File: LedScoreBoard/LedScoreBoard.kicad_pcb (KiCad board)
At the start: 2 copper layers, 145 x 95 mm, 106 parts, among them J1 Conn_01x02_Male, J2 Conn_01x06_Male, J3 Conn_01x02_Male, J4 Conn_01x08_Male, J5 Conn_01x08_Male, J6 Conn_01x08_Male, Q1 BSS84, Q10 BSS84, Q11 BSS138, Q12 BSS84, Q13 BSS138, Q14 2SJ349, Q15 2SJ349, Q16 2SJ349, Q17 TK40E06N1, Q18 TK40E06N1, Q19 TK40E06N1, Q2 BSS84, Q20 TK40E06N1, Q21 BSS138, Q22 BSS138, Q23 BSS138, Q24 BSS138, Q25 TK40E06N1, Q26 TK40E06N1, Q27 TK40E06N1, Q28 BSS138, Q29 BSS138, Q3 BSS84, Q30 BSS138, Q31 BSS138, Q32 BSS138, Q33 BSS138, Q34 BSS138, Q35 BSS138, Q36 BSS138, Q37 BSS138, Q4 BSS138, Q5 BSS138, Q6 BSS138, Q7 BSS138, Q8 BSS84, Q9 BSS138, SW1 SW_Push, SW2 SW_Push, SW3 SW_Push, SW4 SW_Push, SW5 SW_Push, SW6 SW_Push, U1 PIC16F1516-ISP, U2 LM2931-3.3_TO220, U3 LM358, U4 LM358, U5 LM358, U6 LM358

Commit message: SerialTerminal
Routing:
- removed copper zone on F.Cu, net VDD
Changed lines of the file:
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@@
   (segment locked (start 168.91 82.55) (end 163.83 82.55) (width 2) (layer "F.Cu") (net 95))
   (segment locked (start 163.83 66.04) (end 168.91 66.04) (width 2) (layer "F.Cu") (net 96))
-  (zone locked (net 24) (net_name "VDD") (layer "F.Cu") (hatch edge 0.508)
-    (connect_pads (clearance 0.254))
-    (min_thickness 0.254) (filled_areas_thickness no)
-    (fill yes (thermal_gap 0.508) (thermal_bridge_width 0.508))
-    (polygon
-      (pts
-        (xy 161.29 97.79)
-        (xy 156.21 97.79)
-        (xy 156.21 49.53)
-        (xy 161.29 49.53)
-      )
-    )
-  )
   (group "" (id 08d3dc0f-4c91-49b0-ac90-7a56e69acdb1)
     (members

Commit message: 配置ブロック決定
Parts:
- removed C1, C5, C6, C7, C8: 0.1u, Capacitor_SMD:C_0603_1608Metric
- removed C2: 1u, Capacitor_SMD:C_0603_1608Metric
- removed C3, C4: 10u, Capacitor_SMD:C_0603_1608Metric
- removed D1: GDZJ112C, Diode_SMD:D_TUMD2
- removed D2, D3, D4: ER504, Diode_THT:D_DO-27_P5.08mm_Vertical_AnodeUp
- removed DS1: 2831BS-RIGHT-ANGLE, 2831BS-RIGHT-ANGLE:DIPS762W45P254L2253H610Q12N
- removed J1, J3: Conn_01x02_Male, TerminalBlock:TerminalBlock_bornier-2_P5.08mm
- removed J2: Conn_01x06_Male, Connector_PinHeader_2.54mm:PinHeader_1x06_P2.54mm_Vertical
- removed J4, J5, J6: Conn_01x08_Male, Connector_JST:JST_VH_B8P-VH_1x08_P3.96mm_Vertical
- removed Q1, Q10, Q12, Q2, Q3, Q8: BSS84, Package_TO_SOT_SMD:SOT-23_Handsoldering
- removed Q11, Q13, Q21, Q22, Q23, Q24, Q28, Q29, Q30, Q31, Q32, Q33, Q34, Q35, Q36, Q37, Q4, Q5, Q6, Q7, Q9: BSS138, Package_TO_SOT_SMD:SOT-23_Handsoldering
- removed Q14, Q15, Q16: 2SJ349, Package_TO_SOT_THT:TO-220-3_Vertical
- removed Q17, Q18, Q19, Q20, Q25, Q26, Q27: TK40E06N1, Package_TO_SOT_THT:TO-220-3_Vertical
- removed R1, R19, R2, R20, R21, R22, R3, R30, R31, R32, R4, R5, R6, R7: 1k, Resistor_SMD:R_0603_1608Metric
- removed R10, R12, R8: 3.3k, Resistor_SMD:R_0603_1608Metric
- removed R11, R13, R14, R9: 10k, Resistor_SMD:R_0603_1608Metric
- removed R15, R16, R17, R18, R27, R28, R29, R36, R37, R38: 20, Resistor_SMD:R_0603_1608Metric
- removed R23, R24, R25, R26, R33, R34, R35: 1.0, Resistor_SMD:R_2512_6332Metric_Pad1.40x3.35mm_HandSolder
- removed SW1, SW2, SW3, SW4, SW5, SW6: SW_Push, Button_Switch_THT:SW_PUSH_6mm
- removed U1: PIC16F1516-ISP, Package_DIP:DIP-28_W7.62mm_Socket_LongPads
- removed U2: LM2931-3.3_TO220, Package_TO_SOT_THT:TO-220-3_Vertical
- removed U3, U4, U5, U6: LM358, Package_SO:TSSOP-8_3x3mm_P0.65mm
- added C101: 0.1u, Capacitor_SMD:C_0603_1608Metric, F.Cu at (-23.6, 277.4)
- added C102: 0.1u, Capacitor_SMD:C_0603_1608Metric, F.Cu at (24.8, 60.3)
- added C103: 10u, Capacitor_SMD:C_0603_1608Metric, F.Cu at (1.06, 257.0)
- added C104: 10u, Capacitor_SMD:C_0603_1608Metric, F.Cu at (-62.3, 293.9)
- added C201: 1u, Capacitor_SMD:C_0603_1608Metric, B.Cu at (110.2, 30.5)
- added C301: 1u, Capacitor_SMD:C_0603_1608Metric, B.Cu at (35.6, 144.8)
- added C302: 1u, Capacitor_SMD:C_0603_1608Metric, B.Cu at (63.5, 144.8)
- added C303: 1u, Capacitor_SMD:C_0603_1608Metric, B.Cu at (76.2, 144.8)
- added C304: 1u, Capacitor_SMD:C_0603_1608Metric, B.Cu at (104.1, 144.8)
- added C305: 1u, Capacitor_SMD:C_0603_1608Metric, B.Cu at (116.8, 144.8)
- added C306: 1u, Capacitor_SMD:C_0603_1608Metric, B.Cu at (144.8, 144.8)
- added C307: 1u, Capacitor_SMD:C_0603_1608Metric, B.Cu at (157.5, 144.8)
- added C308: 0.1u, Capacitor_SMD:C_0603_1608Metric, B.Cu at (29.2, 152.4)
- added C309: 0.1u, Capacitor_SMD:C_0603_1608Metric, B.Cu at (69.8, 152.4)
- added C310: 0.1u, Capacitor_SMD:C_0603_1608Metric, B.Cu at (110.5, 152.4)
- added C311: 0.1u, Capacitor_SMD:C_0603_1608Metric, B.Cu at (151.1, 152.4)
- added D201: UDZV12B, Diode_SMD:D_TUMD2, B.Cu at (106.3, 30.5)
- added D202: ER504, Diode_THT:D_DO-27_P5.08mm_Vertical_AnodeUp, F.Cu at (125.4, 50.8)
- added D203: ER504, Diode_THT:D_DO-27_P5.08mm_Vertical_AnodeUp, F.Cu at (125.4, 76.2)
- added D204: ER504, Diode_THT:D_DO-27_P5.08mm_Vertical_AnodeUp, F.Cu at (125.4, 101.6)
- added I2C101: Conn_01x04_Male, Connector_PinHeader_2.54mm:PinHeader_1x04_P2.54mm_Vertical, F.Cu at (-23.3, 286.3)
- added J101: LCD, Connector_PinSocket_2.54mm:PinSocket_1x07_P2.54mm_Vertical, F.Cu at (-27.9, 278.5)
- added J102: 1, Connector_JST:JST_VH_B8P-VH_1x08_P3.96mm_Vertical, F.Cu at (137.2, 50.8)
- added J103: 10, Connector_JST:JST_VH_B8P-VH_1x08_P3.96mm_Vertical, F.Cu at (137.2, 76.2)
- added J104: 100, Connector_JST:JST_VH_B8P-VH_1x08_P3.96mm_Vertical, F.Cu at (137.2, 101.6)
- added J105: DC12_IN, TerminalBlock:TerminalBlock_bornier-2_P5.08mm, F.Cu at (-49.5, 291.2)
- added J106: VDD_IN, TerminalBlock:TerminalBlock_bornier-2_P5.08mm, F.Cu at (2.29, 251.2)
- added J107: PICkit, Connector_PinHeader_2.54mm:PinHeader_1x06_P2.54mm_Vertical, F.Cu at (-94.0, 316.2)
- added Q201: BSS138, Package_TO_SOT_SMD:SOT-23_Handsoldering, B.Cu at (86.0, 54.6)
- added Q202: BSS84, Package_TO_SOT_SMD:SOT-23_Handsoldering, B.Cu at (96.2, 47.0)
- added Q203: BSS138, Package_TO_SOT_SMD:SOT-23_Handsoldering, B.Cu at (96.2, 54.6)
- added Q204: 2SJ349, Package_TO_SOT_THT:TO-220-3_Vertical, F.Cu at (108.9, 50.8)
- added Q205: BSS138, Package_TO_SOT_SMD:SOT-23_Handsoldering, B.Cu at (86.0, 80.0)
- added Q206: BSS84, Package_TO_SOT_SMD:SOT-23_Handsoldering, B.Cu at (96.2, 72.4)
- added Q207: BSS138, Package_TO_SOT_SMD:SOT-23_Handsoldering, B.Cu at (96.2, 80.0)
- added Q208: 2SJ349, Package_TO_SOT_THT:TO-220-3_Vertical, F.Cu at (108.9, 76.2)
- added Q209: BSS138, Package_TO_SOT_SMD:SOT-23_Handsoldering, B.Cu at (86.0, 105.4)
- added Q210: BSS84, Package_TO_SOT_SMD:SOT-23_Handsoldering, B.Cu at (96.2, 97.8)
- added Q211: BSS138, Package_TO_SOT_SMD:SOT-23_Handsoldering, B.Cu at (96.2, 105.4)
- added Q212: 2SJ349, Package_TO_SOT_THT:TO-220-3_Vertical, F.Cu at (108.9, 101.6)
- added Q301: BSS138, Package_TO_SOT_SMD:SOT-23_Handsoldering, B.Cu at (35.6, 138.4)
- added Q302: TK40E06N1, Package_TO_SOT_THT:TO-220-3_Vertical, F.Cu at (41.9, 160.0)
- added Q303: BSS138, Package_TO_SOT_SMD:SOT-23_Handsoldering, B.Cu at (63.5, 138.4)
- added Q304: TK40E06N1, Package_TO_SOT_THT:TO-220-3_Vertical, F.Cu at (62.2, 160.0)
- added Q305: BSS138, Package_TO_SOT_SMD:SOT-23_Handsoldering, B.Cu at (76.2, 138.4)
- added Q306: TK40E06N1, Package_TO_SOT_THT:TO-220-3_Vertical, F.Cu at (82.5, 160.0)
- added Q307: BSS138, Package_TO_SOT_SMD:SOT-23_Handsoldering, B.Cu at (104.1, 138.4)
- added Q308: TK40E06N1, Package_TO_SOT_THT:TO-220-3_Vertical, F.Cu at (102.9, 160.0)
- added Q309: BSS138, Package_TO_SOT_SMD:SOT-23_Handsoldering, B.Cu at (116.8, 138.4)
- added Q310: TK40E06N1, Package_TO_SOT_THT:TO-220-3_Vertical, F.Cu at (143.5, 160.0)
- added Q311: BSS138, Package_TO_SOT_SMD:SOT-23_Handsoldering, B.Cu at (144.8, 138.4)
- added Q312: TK40E06N1, Package_TO_SOT_THT:TO-220-3_Vertical, F.Cu at (123.2, 160.0)
- added Q313: BSS138, Package_TO_SOT_SMD:SOT-23_Handsoldering, B.Cu at (157.5, 138.4)
- added Q314: TK40E06N1, Package_TO_SOT_THT:TO-220-3_Vertical, F.Cu at (163.8, 160.0)
- added R201: 3.3k, Resistor_SMD:R_0603_1608Metric, B.Cu at (91.1, 47.0)
- added R202: 10k, Resistor_SMD:R_0603_1608Metric, B.Cu at (91.1, 54.6)
- added R203: 10k, Resistor_SMD:R_0603_1608Metric, B.Cu at (112.7, 30.5)
- added R204: 20, Resistor_SMD:R_0603_1608Metric, B.Cu at (102.5, 50.8)
- added R205: 3.3k, Resistor_SMD:R_0603_1608Metric, B.Cu at (91.1, 72.4)
- added R206: 10k, Resistor_SMD:R_0603_1608Metric, B.Cu at (91.1, 80.0)
- added R207: 20, Resistor_SMD:R_0603_1608Metric, B.Cu at (102.5, 76.2)
- added R208: 3.3k, Resistor_SMD:R_0603_1608Metric, B.Cu at (91.1, 97.8)
- added R209: 10k, Resistor_SMD:R_0603_1608Metric, B.Cu at (91.1, 105.4)
- added R210: 20, Resistor_SMD:R_0603_1608Metric, B.Cu at (102.5, 101.6)
- added R301: 20, Resistor_SMD:R_0603_1608Metric, B.Cu at (35.6, 149.9)
- added R302: 1k, Resistor_SMD:R_0603_1608Metric, B.Cu at (35.6, 147.3)
- added R303: 1.0, Resistor_SMD:R_2512_6332Metric_Pad1.40x3.35mm_HandSolder, B.Cu at (29.2, 160.0)
- added R304: 20, Resistor_SMD:R_0603_1608Metric, B.Cu at (63.5, 149.9)
- added R305: 1k, Resistor_SMD:R_0603_1608Metric, B.Cu at (63.5, 147.3)
- added R306: 1.0, Resistor_SMD:R_2512_6332Metric_Pad1.40x3.35mm_HandSolder, B.Cu at (49.5, 160.0)
- added R307: 20, Resistor_SMD:R_0603_1608Metric, B.Cu at (76.2, 149.9)
- added R308: 1k, Resistor_SMD:R_0603_1608Metric, B.Cu at (76.2, 147.3)
- added R309: 1.0, Resistor_SMD:R_2512_6332Metric_Pad1.40x3.35mm_HandSolder, B.Cu at (69.8, 160.0)
- added R310: 20, Resistor_SMD:R_0603_1608Metric, B.Cu at (104.1, 149.9)
- added R311: 1k, Resistor_SMD:R_0603_1608Metric, B.Cu at (104.1, 147.3)
- added R312: 1.0, Resistor_SMD:R_2512_6332Metric_Pad1.40x3.35mm_HandSolder, B.Cu at (90.2, 160.0)
- added R313: 20, Resistor_SMD:R_0603_1608Metric, B.Cu at (116.8, 149.9)
- added R314: 1k, Resistor_SMD:R_0603_1608Metric, B.Cu at (116.8, 147.3)
- added R315: 1.0, Resistor_SMD:R_2512_6332Metric_Pad1.40x3.35mm_HandSolder, B.Cu at (110.5, 160.0)
- added R316: 20, Resistor_SMD:R_0603_1608Metric, B.Cu at (144.8, 149.9)
- added R317: 1k, Resistor_SMD:R_0603_1608Metric, B.Cu at (144.8, 147.3)
- added R318: 1.0, Resistor_SMD:R_2512_6332Metric_Pad1.40x3.35mm_HandSolder, B.Cu at (130.8, 160.0)
- added R319: 20, Resistor_SMD:R_0603_1608Metric, B.Cu at (157.5, 149.9)
- added R320: 1k, Resistor_SMD:R_0603_1608Metric, B.Cu at (157.5, 147.3)
- added R321: 1.0, Resistor_SMD:R_2512_6332Metric_Pad1.40x3.35mm_HandSolder, B.Cu at (151.1, 160.0)
- added SW101: SW_Push, Button_Switch_THT:SW_PUSH_6mm, F.Cu at (12.6, 248.7)
- added SW102: PlusHun, Button_Switch_THT:SW_PUSH_6mm, F.Cu at (50.8, 91.4)
- added SW103: MinusHun, Button_Switch_THT:SW_PUSH_6mm, F.Cu at (50.8, 101.6)
- added SW104: PlusTen, Button_Switch_THT:SW_PUSH_6mm, F.Cu at (62.2, 91.4)
- added SW105: MinusTen, Button_Switch_THT:SW_PUSH_6mm, F.Cu at (62.2, 101.6)
- added SW106: PlusOne, Button_Switch_THT:SW_PUSH_6mm, F.Cu at (73.7, 91.4)
- added SW107: MinusOne, Button_Switch_THT:SW_PUSH_6mm, F.Cu at (73.7, 101.6)
- added U101: PIC16F1516-ISP, Package_DIP:DIP-28_W7.62mm_Socket_LongPads, F.Cu at (33.0, 121.9)
- added U102: MW-R-WX, MonoWireless:MonoWireless_TWELITE-SMD_SMA-Connector, F.Cu at (38.1, 99.1)
- added U103: LM2931-3.3_TO220, Package_TO_SOT_THT:TO-220-3_Vertical, F.Cu at (-61.1, 290.6)
- added U301: LM358, Package_SO:TSSOP-8_3x3mm_P0.65mm, B.Cu at (29.2, 148.6)
- added U302: LM358, Package_SO:TSSOP-8_3x3mm_P0.65mm, B.Cu at (69.8, 148.6)
- added U303: LM358, Package_SO:TSSOP-8_3x3mm_P0.65mm, B.Cu at (110.5, 148.6)
- added U304: LM358, Package_SO:TSSOP-8_3x3mm_P0.65mm, B.Cu at (151.1, 148.6)
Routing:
- net VDD: track 10.2 -> 0.00 mm
- net /anodeTen: track 8.89 -> 0.00 mm
- net /anodeHun: track 8.89 -> 0.00 mm
- net /anodeOne: track 8.44 -> 0.00 mm
- net Net-(D2-Pad2): track 5.53 -> 0.00 mm
- net Net-(D4-Pad2): track 5.08 -> 0.00 mm
- net Net-(D3-Pad2): track 5.08 -> 0.00 mm
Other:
- board size 145 x 95 mm -> 149.9 x 149.9 mm

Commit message: パターン完成
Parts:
- added J108: TweLite-R, Connector_PinHeader_2.54mm:PinHeader_1x06_P2.54mm_Vertical, F.Cu at (27.9, 78.7)
- added REF01: MountingHole_3.2mm_M3, MountingHole:MountingHole_3.2mm_M3, F.Cu at (25.4, 30.5)
- added REF02: MountingHole_3.2mm_M3, MountingHole:MountingHole_3.2mm_M3, F.Cu at (165.1, 30.5)
- added REF03: MountingHole_3.2mm_M3, MountingHole:MountingHole_3.2mm_M3, F.Cu at (25.4, 170.2)
- added REF04: MountingHole_3.2mm_M3, MountingHole:MountingHole_3.2mm_M3, F.Cu at (165.1, 170.2)
- added REF05: MountingHole_6.4mm_M6, MountingHole:MountingHole_6.4mm_M6, F.Cu at (43.2, 38.1)
- C101, C102, C103, C104: moved to B.Cu
- D202, D203, D204: footprint Diode_THT:D_DO-27_P5.08mm_Vertical_AnodeUp -> Diode_THT:D_DO-27_P12.70mm_Horizontal; moved to B.Cu
- U102: footprint MonoWireless:MonoWireless_TWELITE-SMD_SMA-Connector -> RF_Module:MonoWireless_TWE-L-WX; moved to B.Cu
- moved C104 293.4 mm to (81.3, 38.1), turned to 180 degrees
- moved U103 291.9 mm to (76.2, 33.0)
- moved J105 280.9 mm to (61.0, 33.0)
- moved J106 246.4 mm to (116.8, 33.0)
- moved I2C101 238.5 mm to (27.9, 53.3)
- moved J101 238.1 mm to (33.0, 48.3)
- moved C103 231.4 mm to (76.2, 38.1)
- moved J107 228.3 mm to (27.9, 123.2)
- moved C101 178.1 mm to (50.8, 115.6)
- moved SW101 138.5 mm to (29.5, 111.2), turned to 90 degrees
- moved U101 43.2 mm to (72.4, 104.2), turned to -90 degrees
- moved U102 39.4 mm to (48.3, 61.0), turned to 180 degrees
- moved C102 33.7 mm to (58.4, 61.6), turned to 180 degrees
- moved Q310 20.3 mm to (123.2, 160.0)
- moved Q312 20.3 mm to (143.5, 160.0)
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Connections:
- U102 pad 1: /PlusHun -> unconnected-(U102-Pad1)
- U102 pad 10: unconnected-(U102-Pad10) -> /PlusOne
- U102 pad 11: unconnected-(U102-Pad11) -> /MinusOne
- U102 pad 12: unconnected-(U102-Pad12) -> /PlusTen
- U102 pad 13: unconnected-(U102-Pad13) -> /PlusHun
- U102 pad 15: unconnected-(U102-Pad15) -> /MinusHun
- U102 pad 16: unconnected-(U102-Pad16) -> /MinusTen
- U102 pad 2: /MinusHun -> /PRG
- U102 pad 3: /PlusTen -> unconnected-(U102-Pad3)
- U102 pad 4: /MinusTen -> unconnected-(U102-Pad4)
- U102 pad 6: /PlusOne -> unconnected-(U102-Pad6)
- U102 pad 7: /MinusOne -> unconnected-(U102-Pad7)
- U102 pad 8: unconnected-(U102-Pad8) -> /TX
- U102 pad 9: unconnected-(U102-Pad9) -> /RX
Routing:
- net +12V: track 0.00 -> 329.9 mm, vias 0 -> 4
- net VDD: track 0.00 -> 258.6 mm
- net /LedCathodeDrivers/CathodeA: track 0.00 -> 227.0 mm
- net /LedCathodeDrivers/CathodeB: track 0.00 -> 211.3 mm
- net /LedCathodeDrivers/CathodeC: track 0.00 -> 196.3 mm
- net +3.3V: track 0.00 -> 193.9 mm, vias 0 -> 1
- net /Vref: track 0.00 -> 190.5 mm, vias 0 -> 3
- net /LedCathodeDrivers/CathodeD: track 0.00 -> 181.5 mm
- net /LedCathodeDrivers/CathodeE: track 0.00 -> 166.8 mm
- net /LedCathodeDrivers/CathodeF: track 0.00 -> 151.8 mm
- net /LedCathodeDrivers/CathodeG: track 0.00 -> 135.7 mm
- net /SegmentF: track 0.00 -> 130.4 mm
- net /CsensG: track 0.00 -> 127.4 mm, vias 0 -> 1
- net /SegmentG: track 0.00 -> 126.3 mm, vias 0 -> 1
- net /MCLR: track 0.00 -> 124.8 mm
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- added copper zone on B.Cu, net GND
- added copper zone on F.Cu, net GND

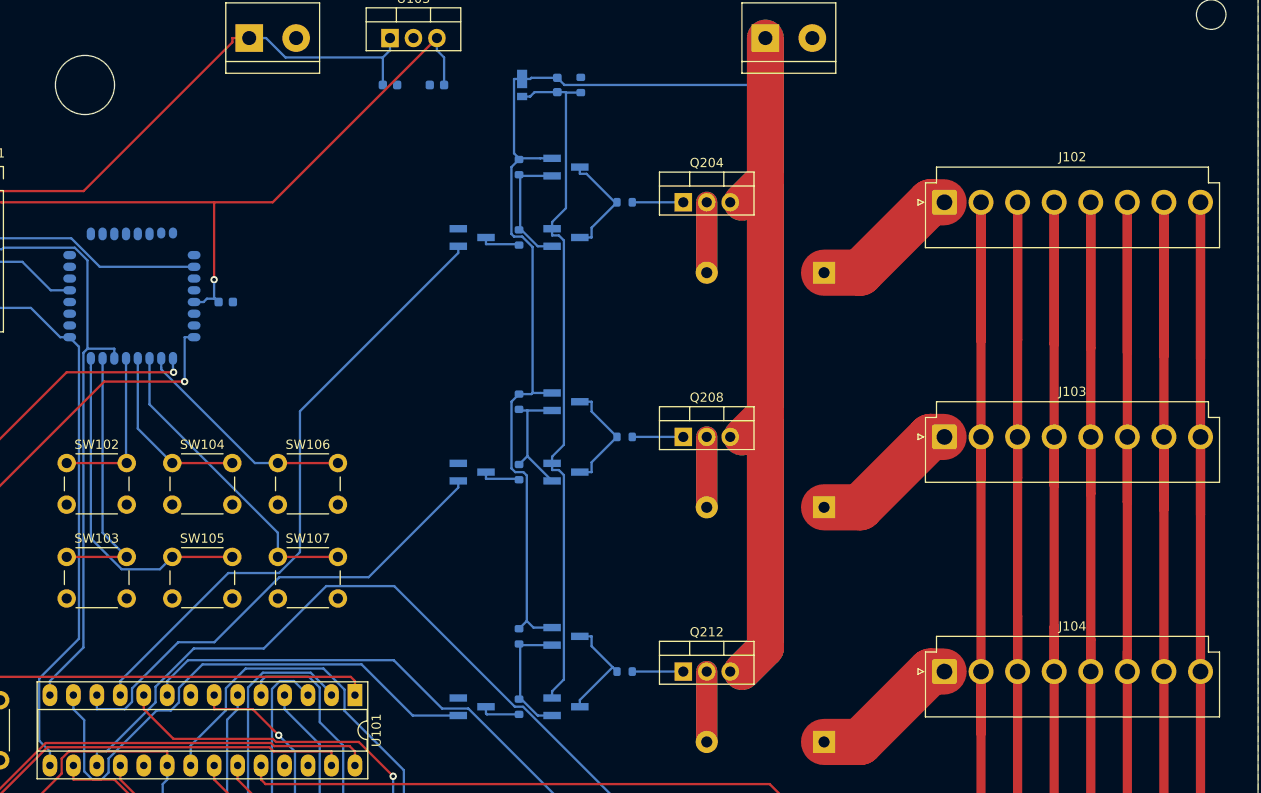
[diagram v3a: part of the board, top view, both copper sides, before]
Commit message: アンテナ穴径修正
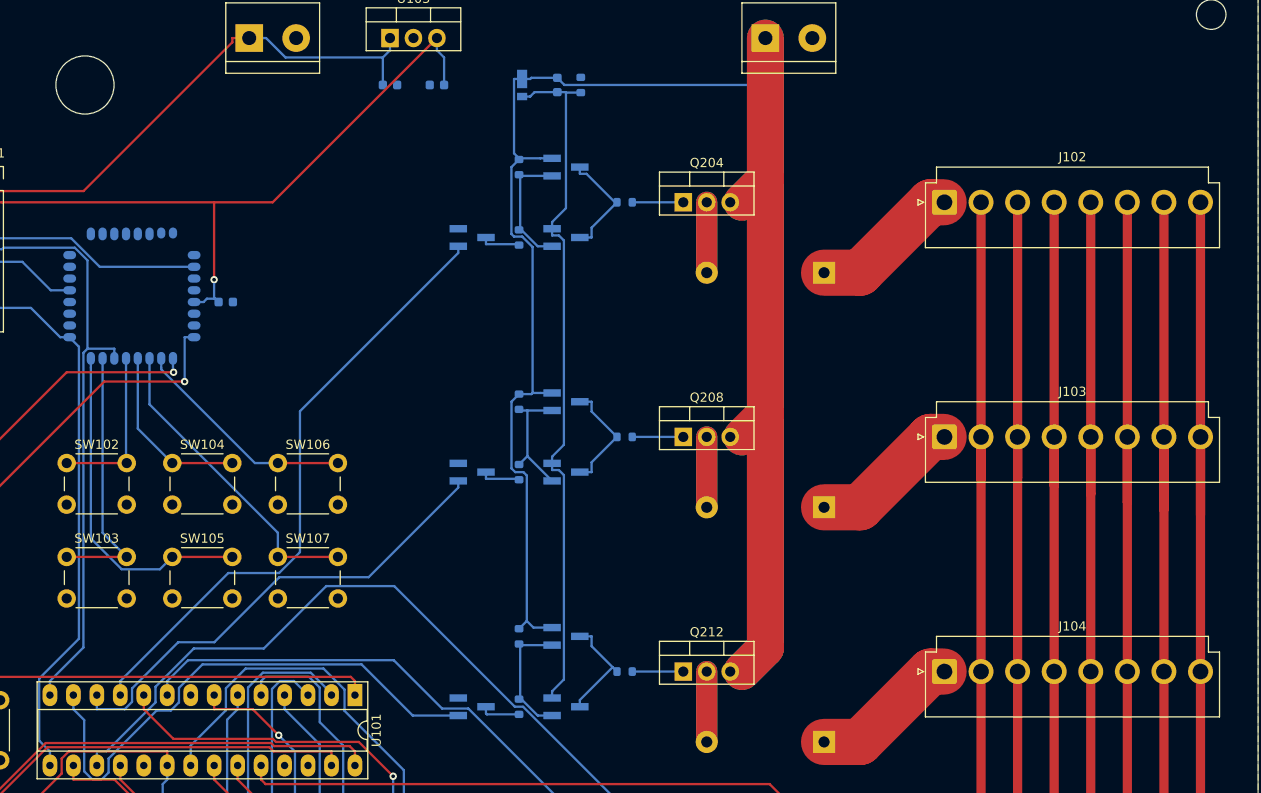
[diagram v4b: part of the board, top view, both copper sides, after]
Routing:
- net /LedCathodeDrivers/CathodeA: track 227.0 -> 205.4 mm
- net /LedCathodeDrivers/CathodeB: track 211.3 -> 190.3 mm
- net /LedCathodeDrivers/CathodeC: track 196.3 -> 176.1 mm
- net /LedCathodeDrivers/CathodeD: track 181.5 -> 162.3 mm
- net /LedCathodeDrivers/CathodeE: track 166.8 -> 148.4 mm
- net /LedCathodeDrivers/CathodeF: track 151.8 -> 134.2 mm
- net /LedCathodeDrivers/CathodeG: track 135.7 -> 118.7 mm
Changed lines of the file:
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@@
     (fp_circle (center 0 0) (end 6.4 0) (layer "Cmts.User") (width 0.15) (fill none))
     (fp_circle (center 0 0) (end 6.65 0) (layer "F.CrtYd") (width 0.05) (fill none))
-    (pad "" np_thru_hole circle locked (at 0 0) (size 6.4 6.4) (drill 6.4) (layers *.Cu *.Mask))
+    (pad "" np_thru_hole circle locked (at 0 0) (size 6.3 6.3) (drill 6.3) (layers F&B.Cu *.Mask))
   )
   (footprint "TerminalBlock:TerminalBlock_bornier-2_P5.08mm" (layer "F.Cu")
@@
   (segment (start 93.75 46.04) (end 92.4747 46.04) (width 0.25) (layer "B.Cu") (net 24))
   (segment (start 91.6348 71.44) (end 91.5098 71.565) (width 0.25) (layer "B.Cu") (net 24))
-  (segment (start 140.1825 108.2801) (end 140.1825 101.6) (width 1) (layer "F.Cu") (net 25))
   (segment locked (start 140.1825 50.8) (end 140.1825 101.6) (width 1) (layer "F.Cu") (net 25))
-  (segment (start 140.182 65.7785) (end 140.1825 65.778) (width 1) (layer "F.Cu") (net 25))
   (segment locked (start 39.37 160.02) (end 39.37 153.67) (width 1) (layer "F.Cu") (net 25))
   (segment locked (start 138.43 139.7) (end 140.1825 137.9475) (width 1) (layer "F.Cu") (net 25))
-  (segment (start 140.1825 65.778) (end 140.1825 50.8) (width 1) (layer "F.Cu") (net 25))
   (segment locked (start 39.37 153.67) (end 53.34 139.7) (width 1) (layer "F.Cu") (net 25))
-  (segment (start 140.182 108.2806) (end 140.1825 108.2801) (width 1) (layer "F.Cu") (net 25))
   (segment locked (start 140.1825 101.6) (end 140.1825 137.9475) (width 1) (layer "F.Cu") (net 25))
   (segment locked (start 53.34 139.7) (end 138.43 139.7) (width 1) (layer "F.Cu") (net 25))
@@
   (segment (start 144.142 80.646) (end 144.1425 80.6455) (width 1) (layer "F.Cu") (net 26))
   (segment locked (start 144.1425 140.3375) (end 144.1425 101.6) (width 1) (layer "F.Cu") (net 26))
-  (segment (start 144.1425 65.7225) (end 144.1425 50.8) (width 1) (layer "F.Cu") (net 26))
-  (segment (start 144.1425 95.5695) (end 144.1425 101.6) (width 1) (layer "F.Cu") (net 26))
-  (segment (start 144.142 95.569) (end 144.1425 95.5695) (width 1) (layer "F.Cu") (net 26))
   (segment (start 144.1425 80.6455) (end 144.1425 76.2) (width 1) (layer "F.Cu") (net 26))
   (segment locked (start 142.24 142.24) (end 144.1425 140.3375) (width 1) (layer "F.Cu") (net 26))
@@
   (segment locked (start 144.1425 101.6) (end 144.1425 50.8) (width 1) (layer "F.Cu") (net 26))
   (segment locked (start 59.69 153.67) (end 71.12 142.24) (width 1) (layer "F.Cu") (net 26))
-  (segment (start 144.142 65.723) (end 144.1425 65.7225) (width 1) (layer "F.Cu") (net 26))
   (segment locked (start 59.69 160.02) (end 59.69 153.67) (width 1) (layer "F.Cu") (net 26))
   (segment locked (start 88.9 144.78) (end 146.05 144.78) (width 1) (layer "F.Cu") (net 27))
@@
   (segment (start 148.1025 81.4421) (end 148.1025 76.2) (width 1) (layer "F.Cu") (net 27))
   (segment (start 148.102 81.4426) (end 148.1025 81.4421) (width 1) (layer "F.Cu") (net 27))
-  (segment (start 148.1025 96.7645) (end 148.1025 101.6) (width 1) (layer "F.Cu") (net 27))
   (segment locked (start 80.01 160.02) (end 80.01 153.67) (width 1) (layer "F.Cu") (net 27))
   (segment locked (start 146.05 144.78) (end 148.1025 142.7275) (width 1) (layer "F.Cu") (net 27))
-  (segment (start 148.1025 66.1208) (end 148.1025 50.8) (width 1) (layer "F.Cu") (net 27))
-  (segment (start 148.102 96.764) (end 148.1025 96.7645) (width 1) (layer "F.Cu") (net 27))
   (segment locked (start 80.01 153.67) (end 88.9 144.78) (width 1) (layer "F.Cu") (net 27))
-  (segment (start 148.102 66.1213) (end 148.1025 66.1208) (width 1) (layer "F.Cu") (net 27))
   (segment locked (start 148.1025 50.8) (end 148.1025 101.6) (width 1) (layer "F.Cu") (net 27))
-  (segment (start 152.0625 98.128) (end 152.0625 101.6) (width 1) (layer "F.Cu") (net 28))
   (segment (start 152.062 82.3516) (end 152.0625 82.3511) (width 1) (layer "F.Cu") (net 28))
-  (segment (start 152.0625 66.5753) (end 152.0625 50.8) (width 1) (layer "F.Cu") (net 28))
   (segment locked (start 152.0625 145.455) (end 152.0625 101.6) (width 1) (layer "F.Cu") (net 28))
   (segment (start 152.0625 82.3511) (end 152.0625 76.2) (width 1) (layer "F.Cu") (net 28))
@@
   (segment locked (start 150.1975 147.32) (end 152.0625 145.455) (width 1) (layer "F.Cu") (net 28))
   (segment locked (start 100.33 153.67) (end 106.68 147.32) (width 1) (layer "F.Cu") (net 28))
-  (segment (start 152.062 66.5758) (end 152.0625 66.5753) (width 1) (layer "F.Cu") (net 28))
   (segment locked (start 152.0625 101.6) (end 152.0625 50.8) (width 1) (layer "F.Cu") (net 28))
-  (segment (start 152.062 98.1275) (end 152.0625 98.128) (width 1) (layer "F.Cu") (net 28))
   (segment locked (start 106.68 147.32) (end 150.1975 147.32) (width 1) (layer "F.Cu") (net 28))
   (segment locked (start 124.46 149.86) (end 154.305 149.86) (width 1) (layer "F.Cu") (net 29))
@@
   (segment locked (start 154.305 149.86) (end 156.0225 148.1425) (width 1) (layer "F.Cu") (net 29))
   (segment locked (start 120.65 160.02) (end 120.65 153.67) (width 1) (layer "F.Cu") (net 29))
-  (segment (start 156.0225 67.0231) (end 156.0225 50.8) (width 1) (layer "F.Cu") (net 29))
-  (segment (start 156.022 99.471) (end 156.0225 99.4715) (width 1) (layer "F.Cu") (net 29))
-  (segment (start 156.0225 99.4715) (end 156.0225 101.6) (width 1) (layer "F.Cu") (net 29))
-  (segment (start 156.022 67.0236) (end 156.0225 67.0231) (width 1) (layer "F.Cu") (net 29))
   (segment locked (start 156.0225 50.8) (end 156.0225 101.6) (width 1) (layer "F.Cu") (net 29))
   (segment (start 156.022 83.2473) (end 156.0225 83.2468) (width 1) (layer "F.Cu") (net 29))
   (segment locked (start 158.115 152.4) (end 159.9825 150.5325) (width 1) (layer "F.Cu") (net 30))
   (segment (start 159.9825 84.0435) (end 159.9825 76.2) (width 1) (layer "F.Cu") (net 30))
-  (segment (start 159.9825 100.6665) (end 159.9825 101.6) (width 1) (layer "F.Cu") (net 30))
-  (segment (start 159.982 67.422) (end 159.9825 67.4215) (width 1) (layer "F.Cu") (net 30))
   (segment locked (start 140.97 153.67) (end 142.24 152.4) (width 1) (layer "F.Cu") (net 30))
-  (segment (start 159.9825 67.4215) (end 159.9825 50.8) (width 1) (layer "F.Cu") (net 30))
   (segment (start 159.982 84.044) (end 159.9825 84.0435) (width 1) (layer "F.Cu") (net 30))
   (segment locked (start 159.9825 150.5325) (end 159.9825 101.6) (width 1) (layer "F.Cu") (net 30))
   (segment locked (start 142.24 152.4) (end 158.115 152.4) (width 1) (layer "F.Cu") (net 30))
-  (segment (start 159.982 100.666) (end 159.9825 100.6665) (width 1) (layer "F.Cu") (net 30))
   (segment locked (start 140.97 160.02) (end 140.97 153.67) (width 1) (layer "F.Cu") (net 30))
   (segment locked (start 159.9825 101.6) (end 159.9825 50.8) (width 1) (layer "F.Cu") (net 30))
-  (segment (start 163.9425 67.7141) (end 163.9425 50.8) (width 1) (layer "F.Cu") (net 31))
-  (segment (start 163.9425 101.5445) (end 163.9425 101.6) (width 1) (layer "F.Cu") (net 31))
   (segment (start 163.942 84.6293) (end 163.9425 84.6288) (width 1) (layer "F.Cu") (net 31))
   (segment locked (start 161.29 160.02) (end 161.29 154.94) (width 1) (layer "F.Cu") (net 31))
-  (segment (start 163.942 101.544) (end 163.9425 101.5445) (width 1) (layer "F.Cu") (net 31))
   (segment (start 163.9425 84.6288) (end 163.9425 76.2) (width 1) (layer "F.Cu") (net 31))
-  (segment (start 163.942 67.7146) (end 163.9425 67.7141) (width 1) (layer "F.Cu") (net 31))
   (segment locked (start 163.9425 152.2875) (end 163.9425 101.6) (width 1) (layer "F.Cu") (net 31))
   (segment locked (start 161.29 154.94) (end 163.9425 152.2875) (width 1) (layer "F.Cu") (net 31))
@@
     (connect_pads (clearance 0))
     (min_thickness 0.2)
-    (keepout (tracks not_allowed) (vias not_allowed) (pads not_allowed ) (copperpour not_allowed) (footprints allowed))
+    (keepout (tracks not_allowed) (vias not_allowed) (pads allowed ) (copperpour not_allowed) (footprints allowed))
     (fill (thermal_gap 0.508) (thermal_bridge_width 0.508))
     (polygon
